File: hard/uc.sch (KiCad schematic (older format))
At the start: 16 parts

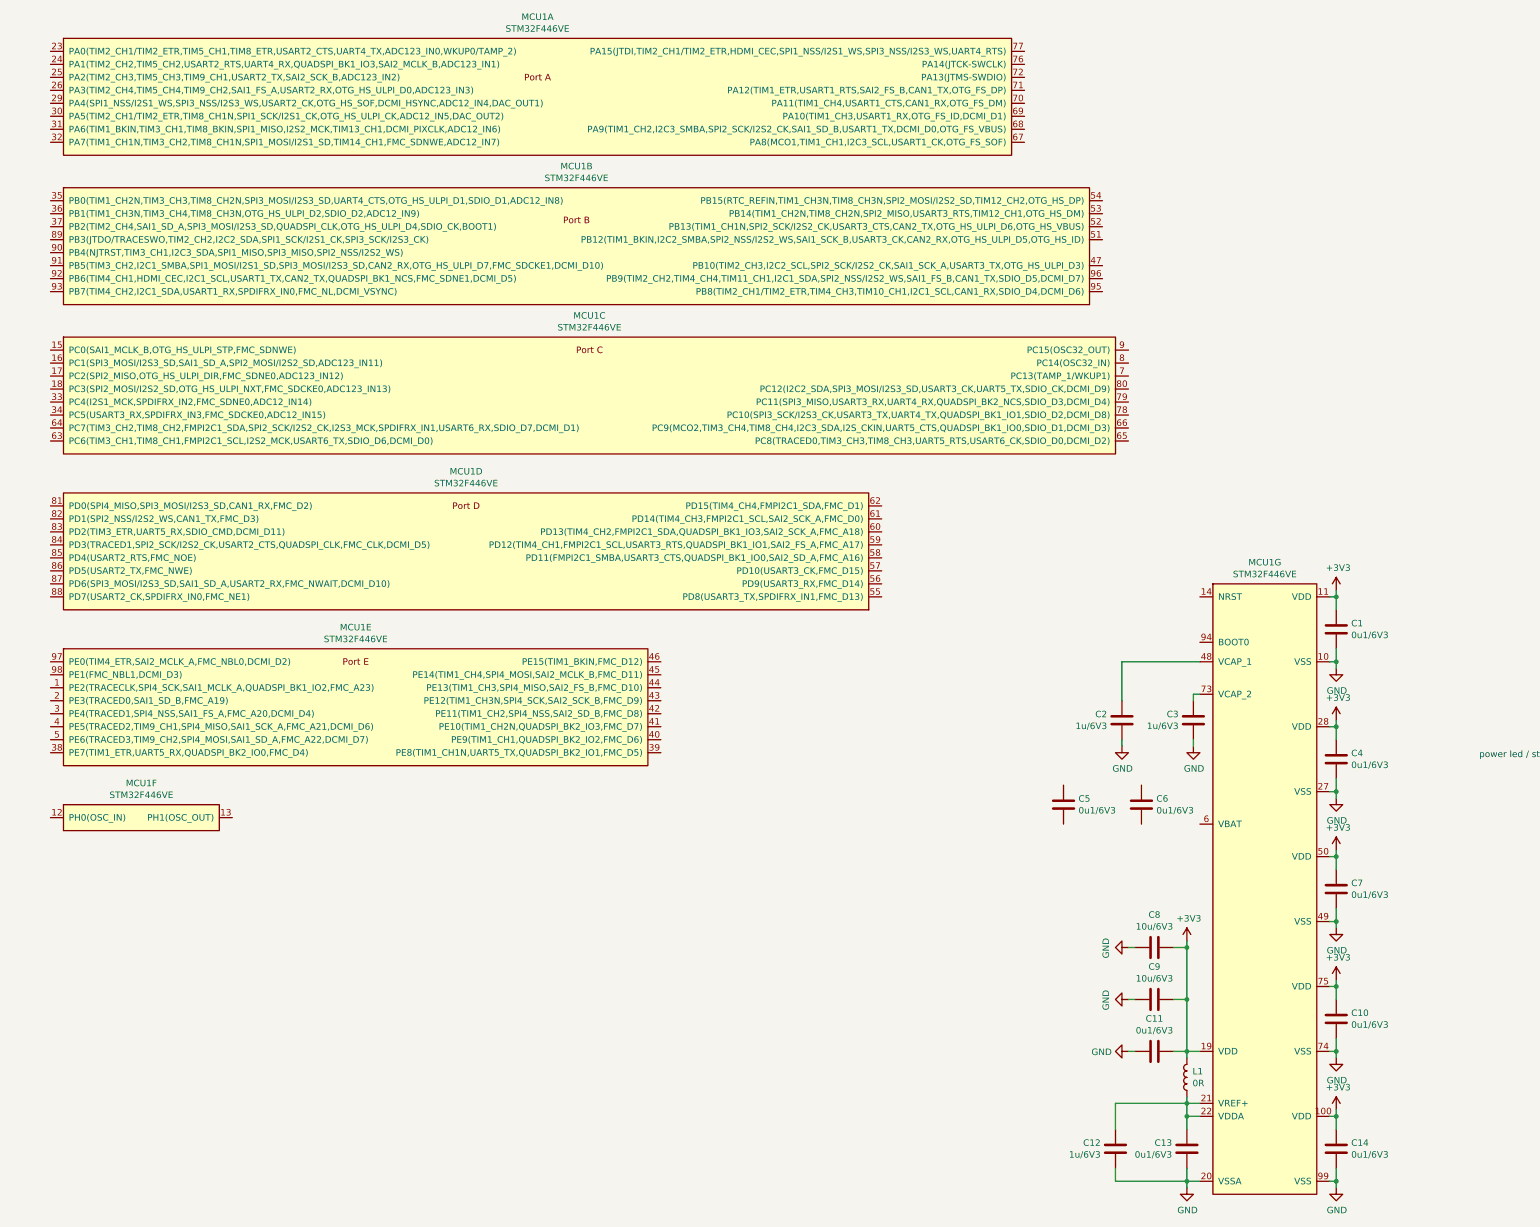
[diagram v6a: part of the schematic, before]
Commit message: uc minimum application
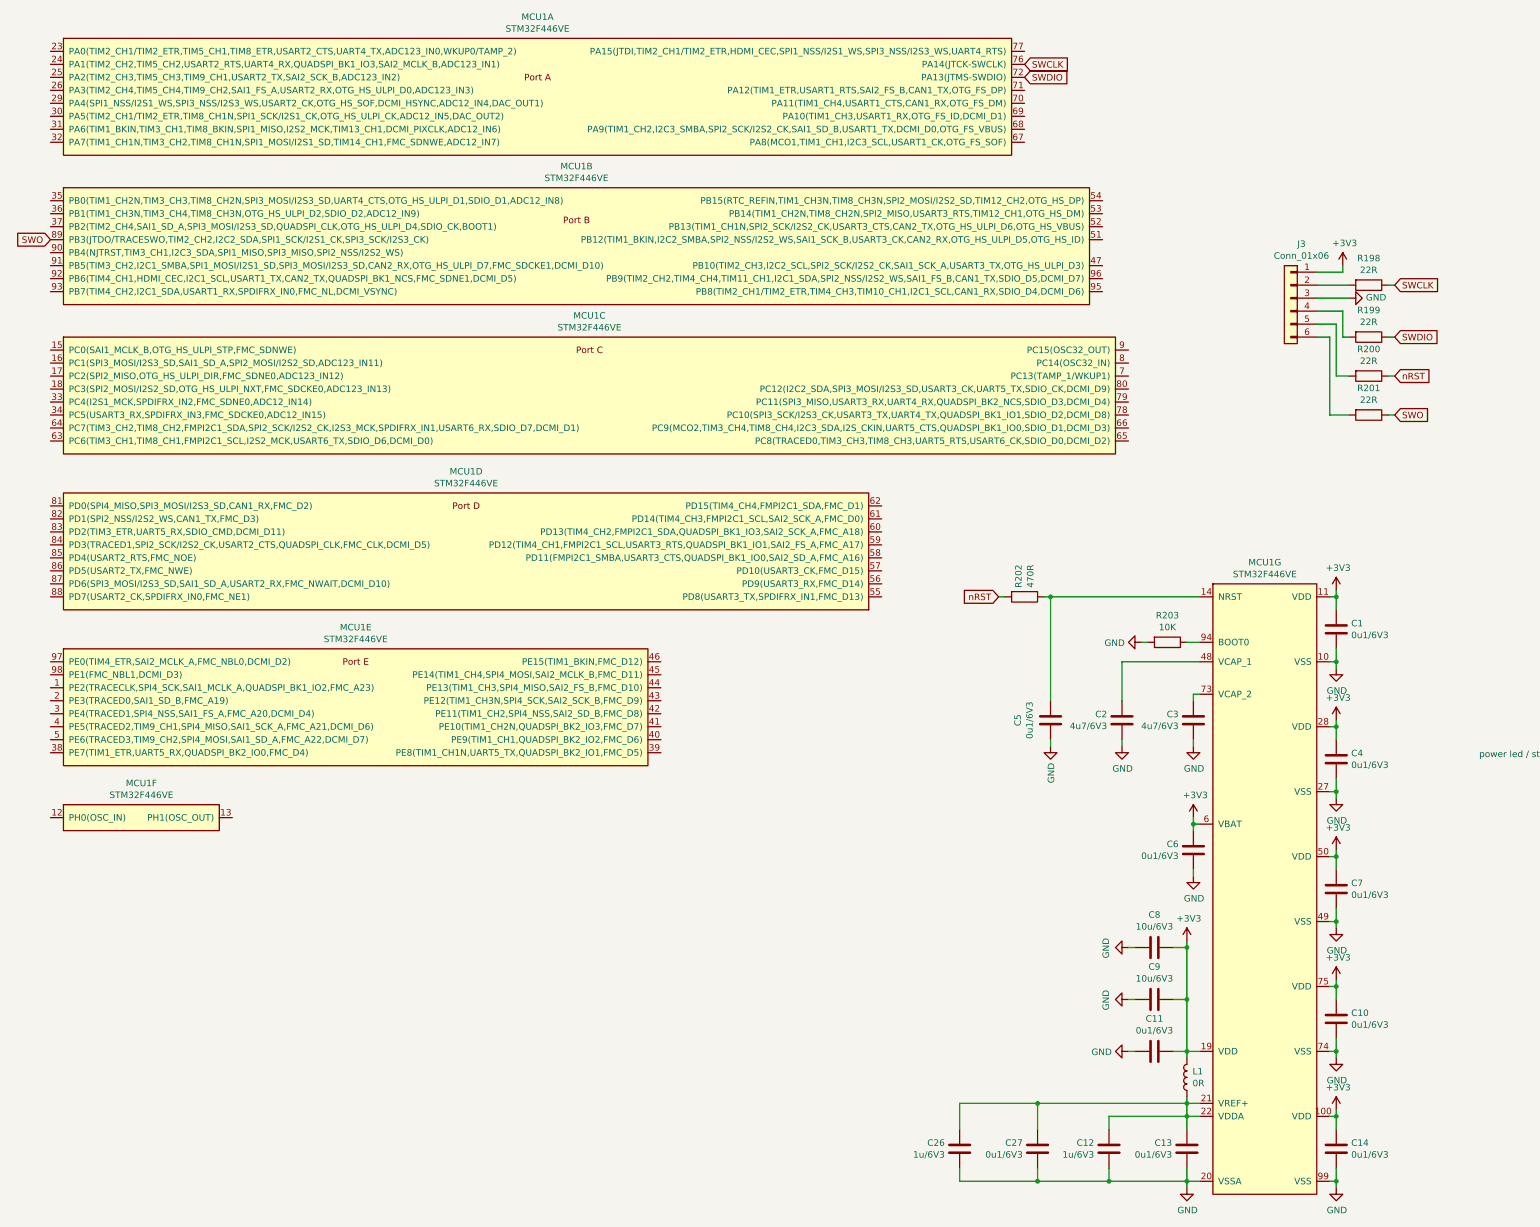
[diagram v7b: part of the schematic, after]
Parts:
- added C26: 1u/6V3, Capacitor_SMD:C_0805_2012Metric, symbol Device:C
- added C27: 0u1/6V3, Capacitor_SMD:C_0402_1005Metric, symbol Device:C
- added J3: Conn_01x06, Connector_PinHeader_2.54mm:PinHeader_1x06_P2.54mm_Horizontal, symbol Connector_Generic:Conn_01x06
- added R198, R199, R200, R201: 22R, Resistor_SMD:R_0402_1005Metric, symbol Device:R
- added R202: 470R, Resistor_SMD:R_0402_1005Metric, symbol Device:R
- added R203: 10K, Resistor_SMD:R_0402_1005Metric, symbol Device:R
- C2, C3: value 1u/6V3 -> 4u7/6V3
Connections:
- net +3V3: now also C6.2, MCU1.6 (VBAT), J3.1 (Pin_1)
- net GND: now also C5.1, C6.1, C26.1, C27.1, J3.3 (Pin_3), R203.2
- net SWDIO: now reaches MCU1.72 (PA13(JTMS-SWDIO))
- net SWDIO: now also R199.1
- net SWCLK: now reaches MCU1.76 (PA14(JTCK-SWCLK))
- net SWCLK: now also R198.1
- net SWO: now reaches MCU1.89 (PB3(JTDO/TRACESWO,TIM2_CH2,I2C2_SDA,SPI1_SCK/I2S1_CK,SPI3_SCK/I2S3_CK))
- net SWO: now also R201.1
- net at MCU1.14 (NRST): now also C5.2, R202.1
- net at C12.2, C13.2, L1.2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: now also C26.2, C27.2
- net at MCU1.94 (BOOT0): now also R203.1
- new net: J3.5 (Pin_5), R200.2
- new net: J3.4 (Pin_4), R199.2
- new net: J3.2 (Pin_2), R198.2
- new net: J3.6 (Pin_6), R201.2
- new net nRST: R200.1, R202.2
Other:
- moved on the sheet: C12, C6

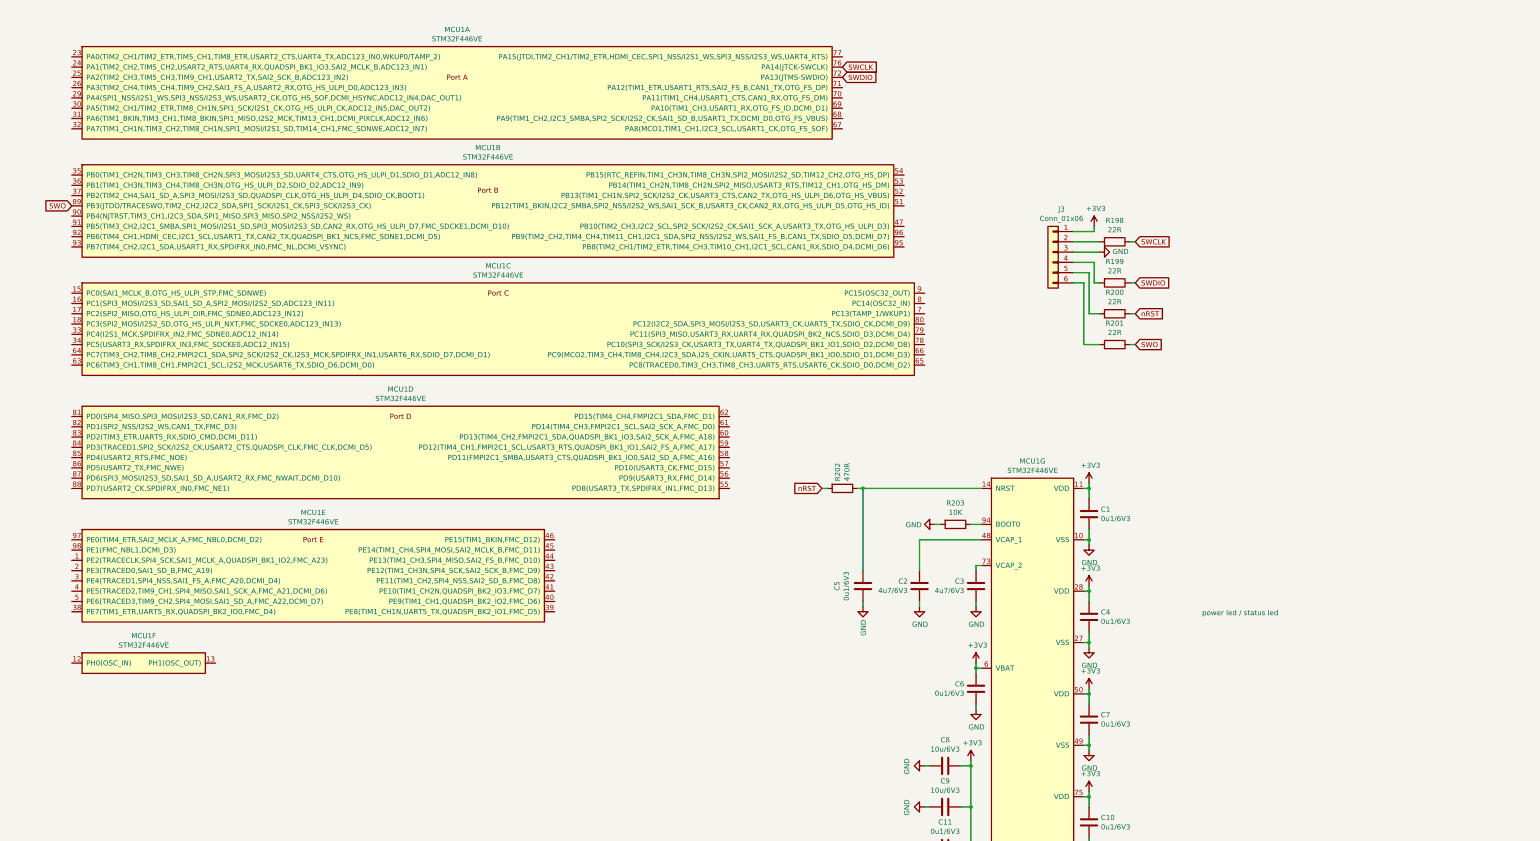
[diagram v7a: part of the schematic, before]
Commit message: connected uc to matrix line driver signals
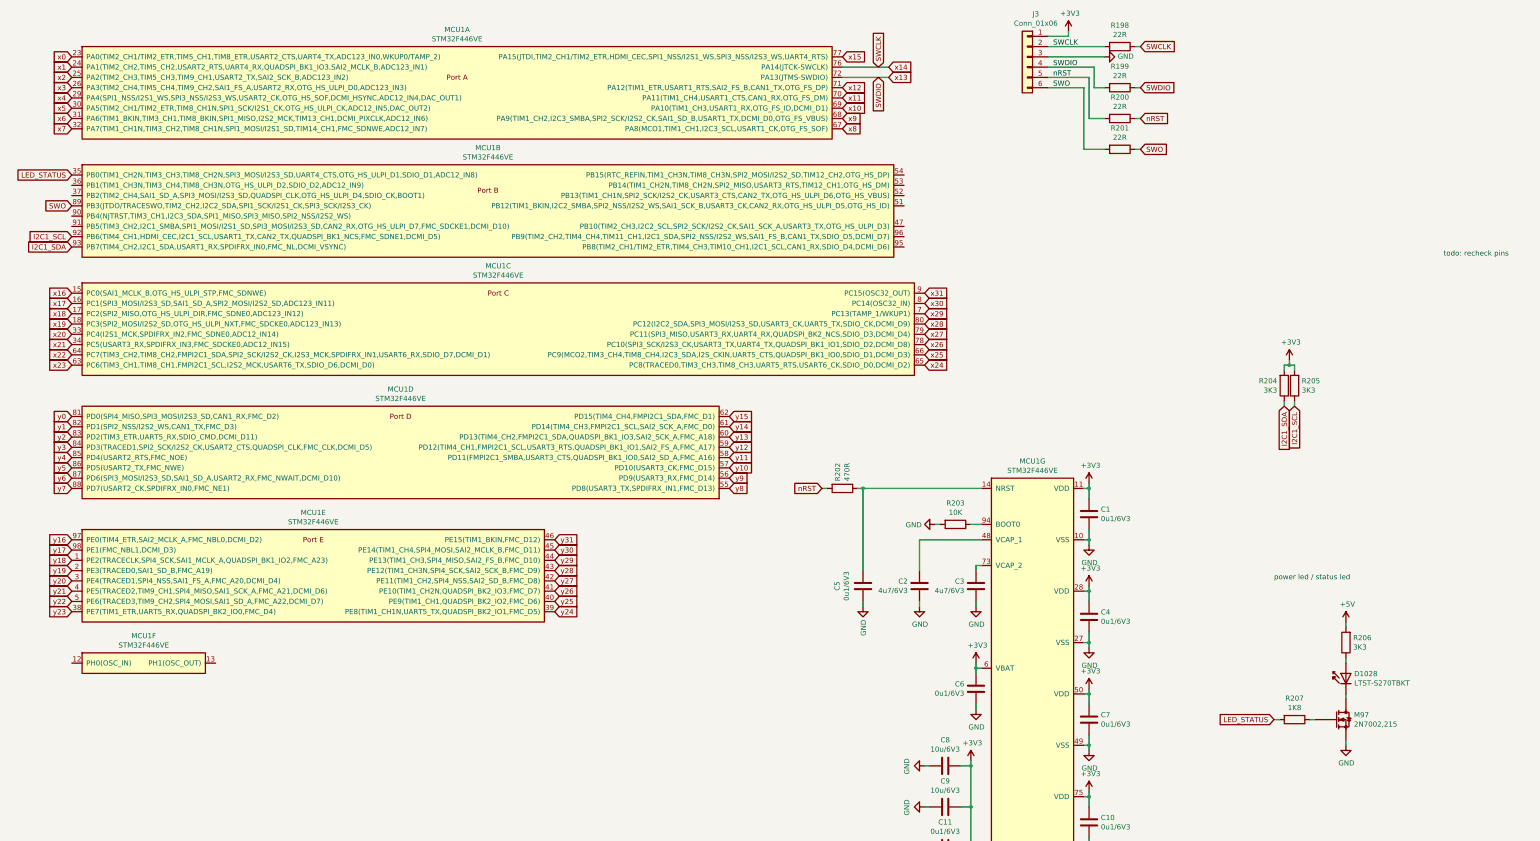
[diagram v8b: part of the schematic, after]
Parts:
- added D1028: LTST-S270TBKT, led_matrix:LED_LiteOn_LTST-S270TBKT, symbol led_matrix:LTST-S270TBKT
- added M97: 2N7002,215, Package_TO_SOT_SMD:SOT-23, symbol led_matrix:2N7002,215
- added R204, R205, R206: 3K3, Resistor_SMD:R_0402_1005Metric, symbol Device:R
- added R207: 1K8, Resistor_SMD:R_0402_1005Metric, symbol Device:R
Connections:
- net +3V3: now also R204.2, R205.2
- net GND: now also M97.2 (S)
- net SWCLK: now also J3.2 (Pin_2), R198.2
- net SWDIO: now also J3.4 (Pin_4), R199.2
- net SWO: now also J3.6 (Pin_6), R201.2
- net nRST: now also J3.5 (Pin_5), R200.2
- net x0: now reaches MCU1.23 (PA0(TIM2_CH1/TIM2_ETR,TIM5_CH1,TIM8_ETR,USART2_CTS,UART4_TX,ADC123_IN0,WKUP0/TAMP_2))
- net x1: now reaches MCU1.24 (PA1(TIM2_CH2,TIM5_CH2,USART2_RTS,UART4_RX,QUADSPI_BK1_IO3,SAI2_MCLK_B,ADC123_IN1))
- net x2: now reaches MCU1.25 (PA2(TIM2_CH3,TIM5_CH3,TIM9_CH1,USART2_TX,SAI2_SCK_B,ADC123_IN2))
- net x3: now reaches MCU1.26 (PA3(TIM2_CH4,TIM5_CH4,TIM9_CH2,SAI1_FS_A,USART2_RX,OTG_HS_ULPI_D0,ADC123_IN3))
- net x4: now reaches MCU1.29 (PA4(SPI1_NSS/I2S1_WS,SPI3_NSS/I2S3_WS,USART2_CK,OTG_HS_SOF,DCMI_HSYNC,ADC12_IN4,DAC_OUT1))
- net x5: now reaches MCU1.30 (PA5(TIM2_CH1/TIM2_ETR,TIM8_CH1N,SPI1_SCK/I2S1_CK,OTG_HS_ULPI_CK,ADC12_IN5,DAC_OUT2))
- net x6: now reaches MCU1.31 (PA6(TIM1_BKIN,TIM3_CH1,TIM8_BKIN,SPI1_MISO,I2S2_MCK,TIM13_CH1,DCMI_PIXCLK,ADC12_IN6))
- net x7: now reaches MCU1.32 (PA7(TIM1_CH1N,TIM3_CH2,TIM8_CH1N,SPI1_MOSI/I2S1_SD,TIM14_CH1,FMC_SDNWE,ADC12_IN7))
- net x8: now reaches MCU1.67 (PA8(MCO1,TIM1_CH1,I2C3_SCL,USART1_CK,OTG_FS_SOF))
- net x9: now reaches MCU1.68 (PA9(TIM1_CH2,I2C3_SMBA,SPI2_SCK/I2S2_CK,SAI1_SD_B,USART1_TX,DCMI_D0,OTG_FS_VBUS))
- net x10: now reaches MCU1.69 (PA10(TIM1_CH3,USART1_RX,OTG_FS_ID,DCMI_D1))
- net x11: now reaches MCU1.70 (PA11(TIM1_CH4,USART1_CTS,CAN1_RX,OTG_FS_DM))
- net x12: now reaches MCU1.71 (PA12(TIM1_ETR,USART1_RTS,SAI2_FS_B,CAN1_TX,OTG_FS_DP))
- net x15: now reaches MCU1.77 (PA15(JTDI,TIM2_CH1/TIM2_ETR,HDMI_CEC,SPI1_NSS/I2S1_WS,SPI3_NSS/I2S3_WS,UART4_RTS))
- net LED_STATUS: now reaches MCU1.35 (PB0(TIM1_CH2N,TIM3_CH3,TIM8_CH2N,SPI3_MOSI/I2S3_SD,UART4_CTS,OTG_HS_ULPI_D1,SDIO_D1,ADC12_IN8))
- net LED_STATUS: now also R207.2
- net I2C1_SCL: now reaches MCU1.92 (PB6(TIM4_CH1,HDMI_CEC,I2C1_SCL,USART1_TX,CAN2_TX,QUADSPI_BK1_NCS,FMC_SDNE1,DCMI_D5))
- net I2C1_SCL: now also R205.1
- net I2C1_SDA: now reaches MCU1.93 (PB7(TIM4_CH2,I2C1_SDA,USART1_RX,SPDIFRX_IN0,FMC_NL,DCMI_VSYNC))
- net I2C1_SDA: now also R204.1
- net x16: now reaches MCU1.15 (PC0(SAI1_MCLK_B,OTG_HS_ULPI_STP,FMC_SDNWE))
- net x17: now reaches MCU1.16 (PC1(SPI3_MOSI/I2S3_SD,SAI1_SD_A,SPI2_MOSI/I2S2_SD,ADC123_IN11))
- net x18: now reaches MCU1.17 (PC2(SPI2_MISO,OTG_HS_ULPI_DIR,FMC_SDNE0,ADC123_IN12))
- net x19: now reaches MCU1.18 (PC3(SPI2_MOSI/I2S2_SD,OTG_HS_ULPI_NXT,FMC_SDCKE0,ADC123_IN13))
- net x20: now reaches MCU1.33 (PC4(I2S1_MCK,SPDIFRX_IN2,FMC_SDNE0,ADC12_IN14))
- net x21: now reaches MCU1.34 (PC5(USART3_RX,SPDIFRX_IN3,FMC_SDCKE0,ADC12_IN15))
- net x23: now reaches MCU1.63 (PC6(TIM3_CH1,TIM8_CH1,FMPI2C1_SCL,I2S2_MCK,USART6_TX,SDIO_D6,DCMI_D0))
- net x22: now reaches MCU1.64 (PC7(TIM3_CH2,TIM8_CH2,FMPI2C1_SDA,SPI2_SCK/I2S2_CK,I2S3_MCK,SPDIFRX_IN1,USART6_RX,SDIO_D7,DCMI_D1))
- net x24: now reaches MCU1.65 (PC8(TRACED0,TIM3_CH3,TIM8_CH3,UART5_RTS,USART6_CK,SDIO_D0,DCMI_D2))
- net x25: now reaches MCU1.66 (PC9(MCO2,TIM3_CH4,TIM8_CH4,I2C3_SDA,I2S_CKIN,UART5_CTS,QUADSPI_BK1_IO0,SDIO_D1,DCMI_D3))
- net x29: now reaches MCU1.7 (PC13(TAMP_1/WKUP1))
- net x26: now reaches MCU1.78 (PC10(SPI3_SCK/I2S3_CK,USART3_TX,UART4_TX,QUADSPI_BK1_IO1,SDIO_D2,DCMI_D8))
- net x27: now reaches MCU1.79 (PC11(SPI3_MISO,USART3_RX,UART4_RX,QUADSPI_BK2_NCS,SDIO_D3,DCMI_D4))
- net x30: now reaches MCU1.8 (PC14(OSC32_IN))
- net x28: now reaches MCU1.80 (PC12(I2C2_SDA,SPI3_MOSI/I2S3_SD,USART3_CK,UART5_TX,SDIO_CK,DCMI_D9))
- net x31: now reaches MCU1.9 (PC15(OSC32_OUT))
- net y8: now reaches MCU1.55 (PD8(USART3_TX,SPDIFRX_IN1,FMC_D13))
- net y9: now reaches MCU1.56 (PD9(USART3_RX,FMC_D14))
- net y10: now reaches MCU1.57 (PD10(USART3_CK,FMC_D15))
- net y11: now reaches MCU1.58 (PD11(FMPI2C1_SMBA,USART3_CTS,QUADSPI_BK1_IO0,SAI2_SD_A,FMC_A16))
- net y12: now reaches MCU1.59 (PD12(TIM4_CH1,FMPI2C1_SCL,USART3_RTS,QUADSPI_BK1_IO1,SAI2_FS_A,FMC_A17))
- net y13: now reaches MCU1.60 (PD13(TIM4_CH2,FMPI2C1_SDA,QUADSPI_BK1_IO3,SAI2_SCK_A,FMC_A18))
- net y14: now reaches MCU1.61 (PD14(TIM4_CH3,FMPI2C1_SCL,SAI2_SCK_A,FMC_D0))
- net y15: now reaches MCU1.62 (PD15(TIM4_CH4,FMPI2C1_SDA,FMC_D1))
- net y0: now reaches MCU1.81 (PD0(SPI4_MISO,SPI3_MOSI/I2S3_SD,CAN1_RX,FMC_D2))
- net y1: now reaches MCU1.82 (PD1(SPI2_NSS/I2S2_WS,CAN1_TX,FMC_D3))
- net y2: now reaches MCU1.83 (PD2(TIM3_ETR,UART5_RX,SDIO_CMD,DCMI_D11))
- net y3: now reaches MCU1.84 (PD3(TRACED1,SPI2_SCK/I2S2_CK,USART2_CTS,QUADSPI_CLK,FMC_CLK,DCMI_D5))
- net y4: now reaches MCU1.85 (PD4(USART2_RTS,FMC_NOE))
- net y5: now reaches MCU1.86 (PD5(USART2_TX,FMC_NWE))
- net y6: now reaches MCU1.87 (PD6(SPI3_MOSI/I2S3_SD,SAI1_SD_A,USART2_RX,FMC_NWAIT,DCMI_D10))
- net y7: now reaches MCU1.88 (PD7(USART2_CK,SPDIFRX_IN0,FMC_NE1))
- net y18: now reaches MCU1.1 (PE2(TRACECLK,SPI4_SCK,SAI1_MCLK_A,QUADSPI_BK1_IO2,FMC_A23))
- net y19: now reaches MCU1.2 (PE3(TRACED0,SAI1_SD_B,FMC_A19))
- net y20: now reaches MCU1.3 (PE4(TRACED1,SPI4_NSS,SAI1_FS_A,FMC_A20,DCMI_D4))
- net y23: now reaches MCU1.38 (PE7(TIM1_ETR,UART5_RX,QUADSPI_BK2_IO0,FMC_D4))
- net y24: now reaches MCU1.39 (PE8(TIM1_CH1N,UART5_TX,QUADSPI_BK2_IO1,FMC_D5))
- net y21: now reaches MCU1.4 (PE5(TRACED2,TIM9_CH1,SPI4_MISO,SAI1_SCK_A,FMC_A21,DCMI_D6))
- net y25: now reaches MCU1.40 (PE9(TIM1_CH1,QUADSPI_BK2_IO2,FMC_D6))
- net y26: now reaches MCU1.41 (PE10(TIM1_CH2N,QUADSPI_BK2_IO3,FMC_D7))
- net y27: now reaches MCU1.42 (PE11(TIM1_CH2,SPI4_NSS,SAI2_SD_B,FMC_D8))
- net y28: now reaches MCU1.43 (PE12(TIM1_CH3N,SPI4_SCK,SAI2_SCK_B,FMC_D9))
- net y29: now reaches MCU1.44 (PE13(TIM1_CH3,SPI4_MISO,SAI2_FS_B,FMC_D10))
- net y30: now reaches MCU1.45 (PE14(TIM1_CH4,SPI4_MOSI,SAI2_MCLK_B,FMC_D11))
- net y31: now reaches MCU1.46 (PE15(TIM1_BKIN,FMC_D12))
- net y22: now reaches MCU1.5 (PE6(TRACED3,TIM9_CH2,SPI4_MOSI,SAI1_SD_A,FMC_A22,DCMI_D7))
- net y16: now reaches MCU1.97 (PE0(TIM4_ETR,SAI2_MCLK_A,FMC_NBL0,DCMI_D2))
- net y17: now reaches MCU1.98 (PE1(FMC_NBL1,DCMI_D3))
- new net: D1028.A, R206.1
- new net: D1028.C, M97.3 (D)
- new net: M97.1 (G), R207.1
- new net +5V: R206.2
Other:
- note added: "todo: recheck pins\n"
- moved on the sheet: J3, R198, R199, R200, R201
